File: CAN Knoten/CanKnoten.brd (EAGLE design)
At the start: 112.9 x 61.3 mm, 43 parts, among them IC1 74LS165D, IC2 74LS165D, K1 68711614522, K2 68711614522, K3 68711614522, K4 68711614522, Q1 HC49-U - 16MHz, Q2 HC49-U - xMHz

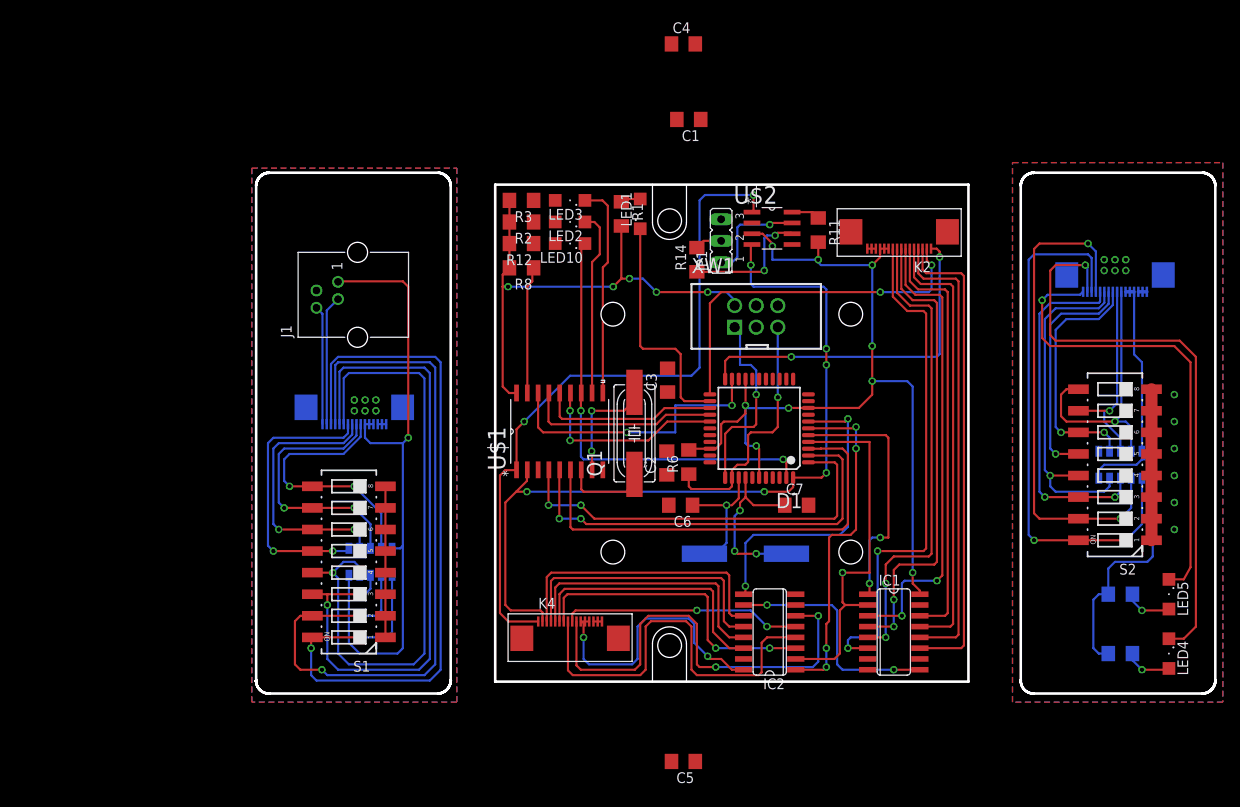
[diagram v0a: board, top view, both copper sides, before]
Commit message: 
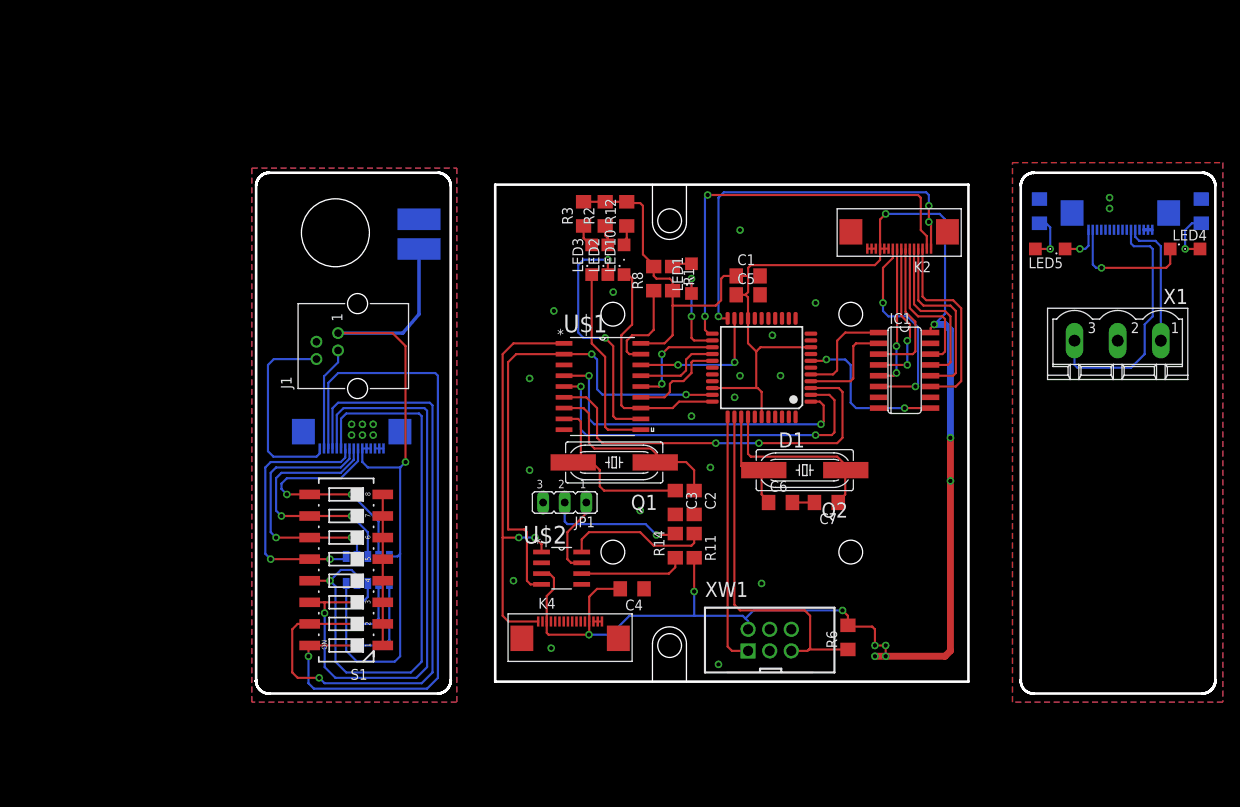
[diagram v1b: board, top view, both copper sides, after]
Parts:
- removed IC2: 74LS165D, 74xx-us:SO16
- removed RN1: (no value), resistor-array:745-10
- removed S2: 219-08, switch-dil:CTS-219-08
- added PAD1, PAD2: (no value), wirepad:SMD2,54-5,08
- added X1: MSTBV3, con-phoenix-508:MSTBV3
- moved C4 64.4 mm to (62.9, -29.2), turned to 180 degrees
- moved C5 55.5 mm to (76.5, 5.40), turned to 0 degrees
- moved R4 52.9 mm to (129.9, 15.2), turned to 90 degrees
- moved LED4 47.7 mm to (128.0, 10.8), turned to 0 degrees
- moved U$2 47.1 mm to (54.6, -26.8)
- moved R5 46.1 mm to (110.8, 15.2), turned to 90 degrees
- moved LED5 43.0 mm to (112.1, 10.8), turned to 180 degrees
- moved R11 39.9 mm to (70.2, -24.1)
- moved XW1 38.1 mm to (79.1, -35.2)
- moved JP1 35.9 mm to (54.9, -19.1), turned to 180 degrees
- moved R14 33.8 mm to (67.9, -24.1)
- moved IC1 30.8 mm to (94.9, -3.49)
- moved R6 27.9 mm to (88.3, -34.9)
- moved C1 19.7 mm to (76.5, 7.62), turned to 0 degrees
- moved U$4 19.1 mm to (95.2, -29.2)
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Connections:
- net N$31 renamed PDI_RESET
- net N$33 renamed REAR_MCP2515_TXCAN
- net N$34 renamed REAR_MCP2515_RXCAN
- removed net 74XX165_SH/LD_IC2: D1.6, IC2.1
- removed net CAN_BITRATE_0: IC2.11, K4.3
- removed net CAN_BITRATE_1: IC2.12, K4.4
- removed net CAN_BITRATE_2: IC2.13, K4.5
- removed net CAN_BITRATE_3: IC2.14, K4.6
- removed net CAN_BITRATE_4: IC2.3, K4.7
- removed net CAN_BITRATE_5: IC2.4, K4.8
- removed net CAN_BITRATE_6: IC2.5, K4.9
- removed net CAN_BITRATE_7: IC2.6, K4.10
- removed net N$13: D1.40
- removed net N$14: D1.41
- removed net N$18: D1.42
- removed net N$19: K3.9, RN1.8, S2.10
- removed net N$2: IC1.9, IC2.10
- removed net N$20: D1.28
- removed net N$21: D1.29
- removed net N$30: K3.10, RN1.9, S2.9
- removed net N$4: K3.3, RN1.1, S2.16
- removed net N$5: K3.4, RN1.2, S2.15
- removed net N$6: K3.5, RN1.3, S2.14
- removed net N$7: K3.6, RN1.4, S2.13
- removed net N$8: K3.7, RN1.6, S2.12
- removed net N$9: K3.8, RN1.7, S2.11
- new net REAR_CANH: K3.12, X1.1
- new net REAR_CANL: K3.11, X1.3
- net 74XX165_CLK: no longer IC2.2
- net 74XX165_OUT: now also IC1.9; no longer IC2.9
- net FRONT_GND: now also PAD1.1
- net FRONT_VCC: now also PAD2.1
- net GND: now also IC1.10; no longer IC2.15, IC2.8
- net MCP2515_INT: now also D1.33; no longer D1.43
- net MCP2515_RXCAN: now also D1.32; no longer D1.44
- net REAR_GND: now also X1.2; no longer S2.1, S2.2, S2.3, S2.4, S2.5, S2.6, S2.7, S2.8
- net REAR_VCC: now also K3.3; no longer K3.11, K3.12, RN1.10, RN1.5
- net VCC: now also K4.3; no longer IC2.16, K4.11, K4.12
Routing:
- net N$4: track 64.0 -> 0.00 mm, vias 2 -> 0
- net N$5: track 59.5 -> 0.00 mm, vias 2 -> 0
- net REAR_VCC: track 58.6 -> 0.00 mm
- net REAR_MCP2515_RXCAN: track 69.0 -> 15.3 mm
- net CAN_BITRATE_7: track 52.8 -> 0.00 mm, vias 2 -> 0
- net REAR_MCP2515_TXCAN: track 55.8 -> 4.79 mm
- net CAN_BITRATE_5: track 47.9 -> 0.00 mm
- net N$6: track 41.5 -> 0.00 mm, vias 2 -> 0
- net N$7: track 40.8 -> 0.00 mm, vias 1 -> 0
- net 74XX165_SH/LD_IC2: track 40.4 -> 0.00 mm, vias 4 -> 0
- net NODE_ID_6: track 55.5 -> 16.9 mm
- net VCC: track 199.5 -> 237.9 mm, vias 16 -> 11
- net MCP2515_RXCAN: track 96.3 -> 58.1 mm, vias 6 -> 2
- net NODE_ID_4: track 54.9 -> 17.1 mm, vias 2 -> 0
- net NODE_ID_5: track 55.3 -> 17.6 mm
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
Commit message: 
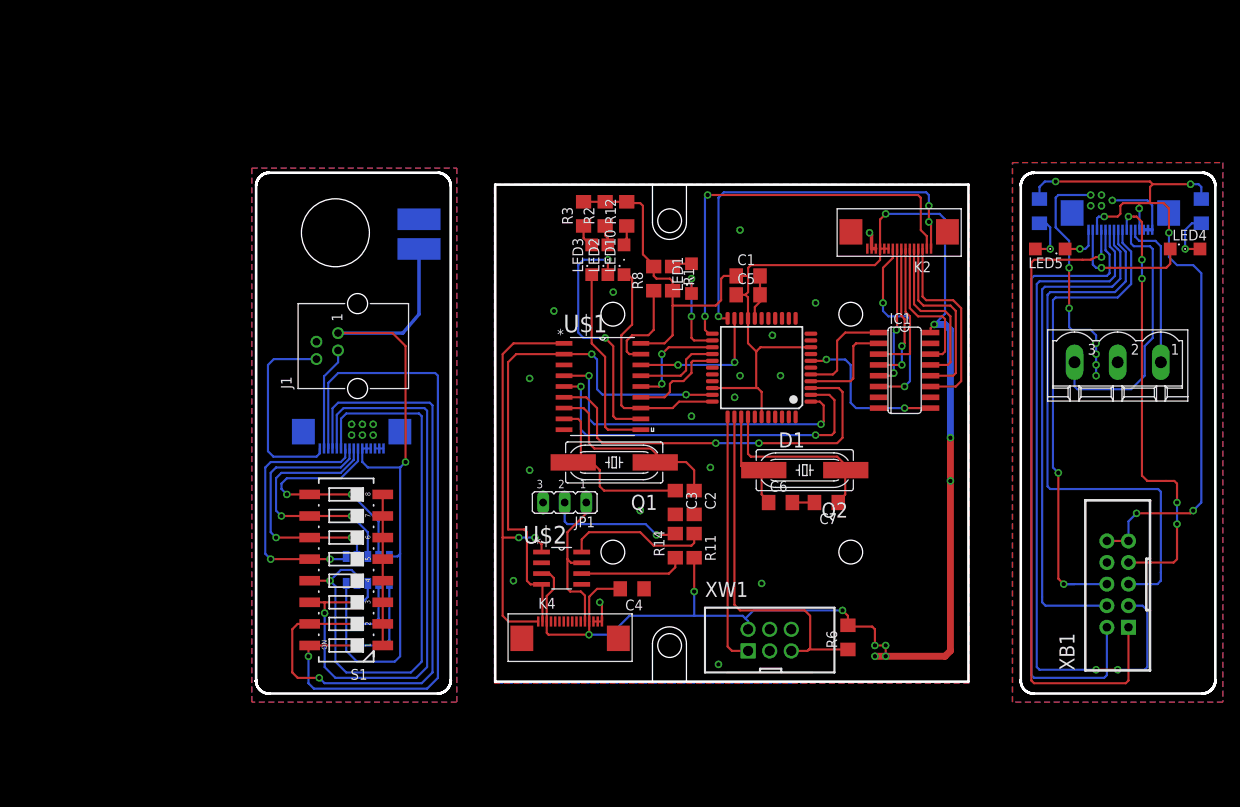
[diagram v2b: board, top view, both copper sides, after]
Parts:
- added XB1: (no value), Wannenstiftleisten:WSL10
- moved X1 2.54 mm to (120.0, -2.54)
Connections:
- removed net N$17: C6.2, C7.2
- new net EXTENDED_I2C_SCL: D1.11, K4.7
- new net EXTENDED_I2C_SDA: D1.10, K4.6
- new net EXTENDED_SPI_MISO: D1.16, K4.8
- new net EXTENDED_SPI_MOSI: D1.15, K4.9
- new net EXTENDED_SPI_SCK: D1.17, K4.10
- new net EXTENDED_UART_RXD: D1.12, K4.4
- new net EXTENDED_UART_TXD: D1.13, K4.5
- new net N$2: K3.4, XB1.1
- new net N$4: K3.5, XB1.2
- new net N$5: K3.6, XB1.3
- new net N$6: K3.7, XB1.4
- new net N$7: K3.8, XB1.5
- new net N$8: K3.9, XB1.6
- new net N$9: K3.10, XB1.7
- net GND: now also C6.2, C7.2
- net MCP2551_CANH: now also K4.12
- net MCP2551_CANL: now also K4.11
- net REAR_GND: now also XB1.8
- net REAR_VCC: now also XB1.10, XB1.9
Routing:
- net REAR_VCC: track 0.00 -> 91.0 mm, vias 0 -> 7
- net N$5: track 0.00 -> 82.8 mm, vias 0 -> 2
- net N$2: track 0.00 -> 78.8 mm, vias 0 -> 1
- net N$4: track 0.00 -> 76.2 mm
- net N$7: track 0.00 -> 66.9 mm
- net N$6: track 0.00 -> 60.4 mm
- net N$8: track 0.00 -> 57.1 mm, vias 0 -> 2
- net N$9: track 0.00 -> 52.7 mm, vias 0 -> 5
- net REAR_GND: track 1.00 -> 37.3 mm, vias 2 -> 11
- net GND: track 2.00 -> 13.8 mm, vias 17 -> 18
- net MCP2551_CANH: track 9.67 -> 18.6 mm
- net MCP2515_RXCAN: track 58.1 -> 62.5 mm
- net N$17: track 2.60 -> 0.00 mm
- net REAR_CANL: track 29.1 -> 31.7 mm
- net REAR_CANH: track 15.4 -> 18.0 mm
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- added copper zone on layer 1, net GND
- added copper zone on layer 16, net GND
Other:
- board text added: "CAN-H"
- board text added: "CAN-L"
- board text added: "GND"

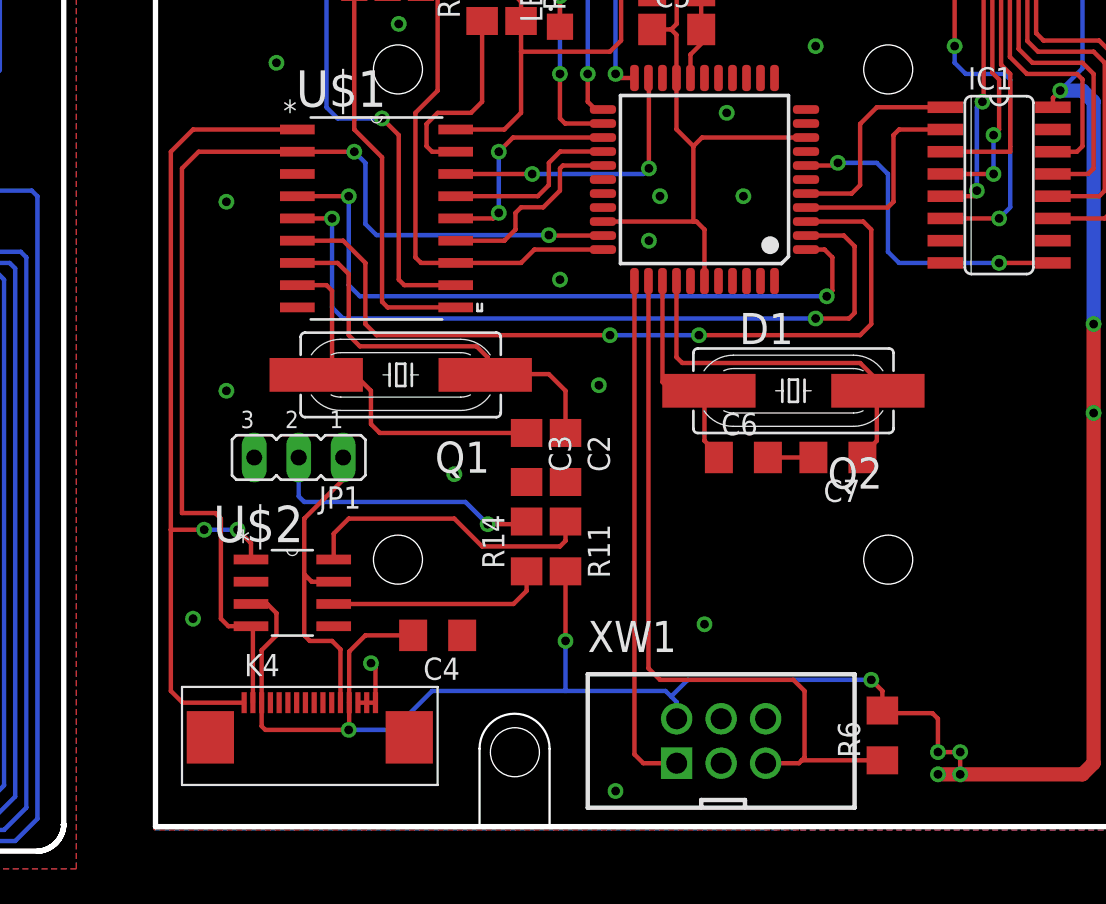
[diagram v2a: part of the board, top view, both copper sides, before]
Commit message: 
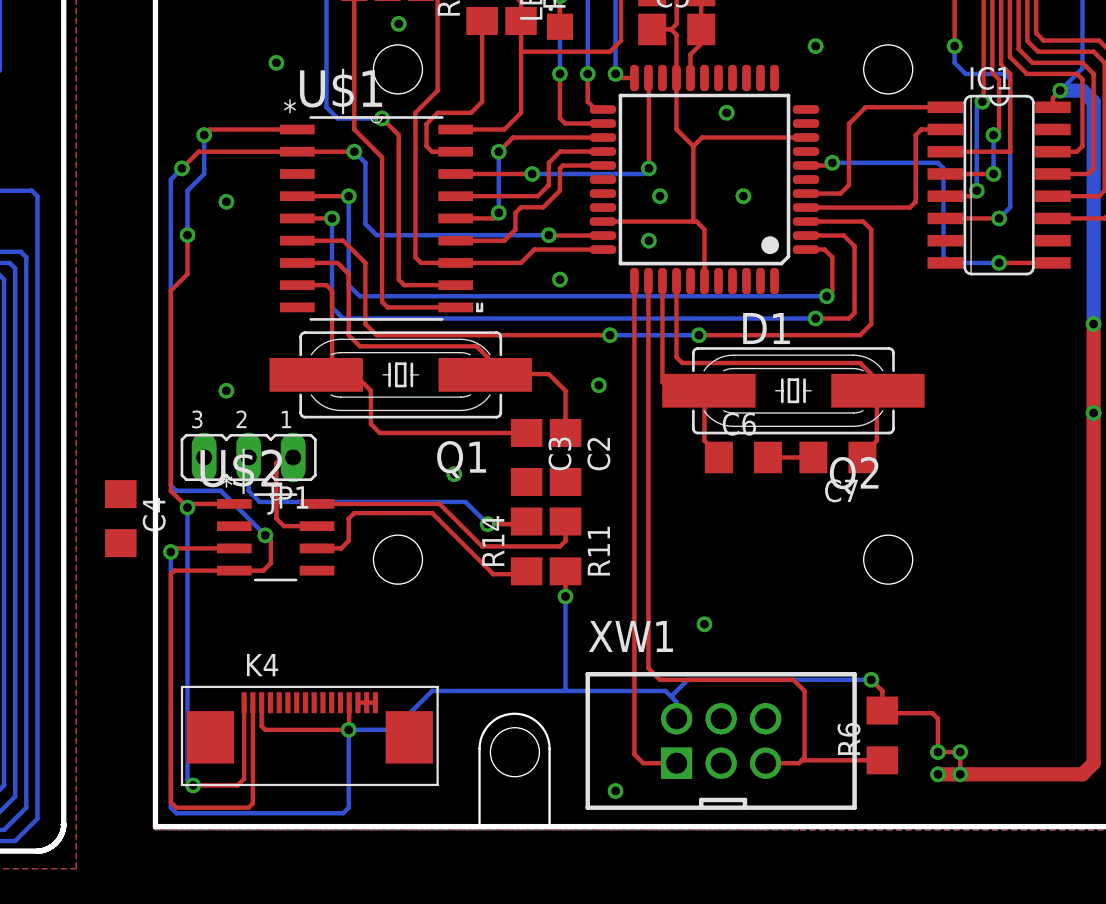
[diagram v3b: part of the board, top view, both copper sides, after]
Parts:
- moved C4 19.3 mm to (44.8, -22.5), turned to 270 degrees
- moved U$2 3.31 mm to (53.6, -23.6)
- moved JP1 2.86 mm to (52.1, -19.1)
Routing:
- net MCP2515_RXCAN: track 62.5 -> 84.8 mm, vias 2 -> 4
- net VCC: track 237.9 -> 257.0 mm, vias 11 -> 12
- net MCP2551_CANH: track 18.6 -> 6.75 mm
- net MCP2515_TXCAN: track 48.8 -> 54.1 mm, vias 2 -> 4
- net N$12: track 16.0 -> 18.6 mm
- net MCP2551_CANL: track 12.4 -> 15.1 mm
- net GND: track 13.8 -> 11.5 mm, vias 18 -> 16
- net MCP2551_RS: track 17.0 -> 16.4 mm

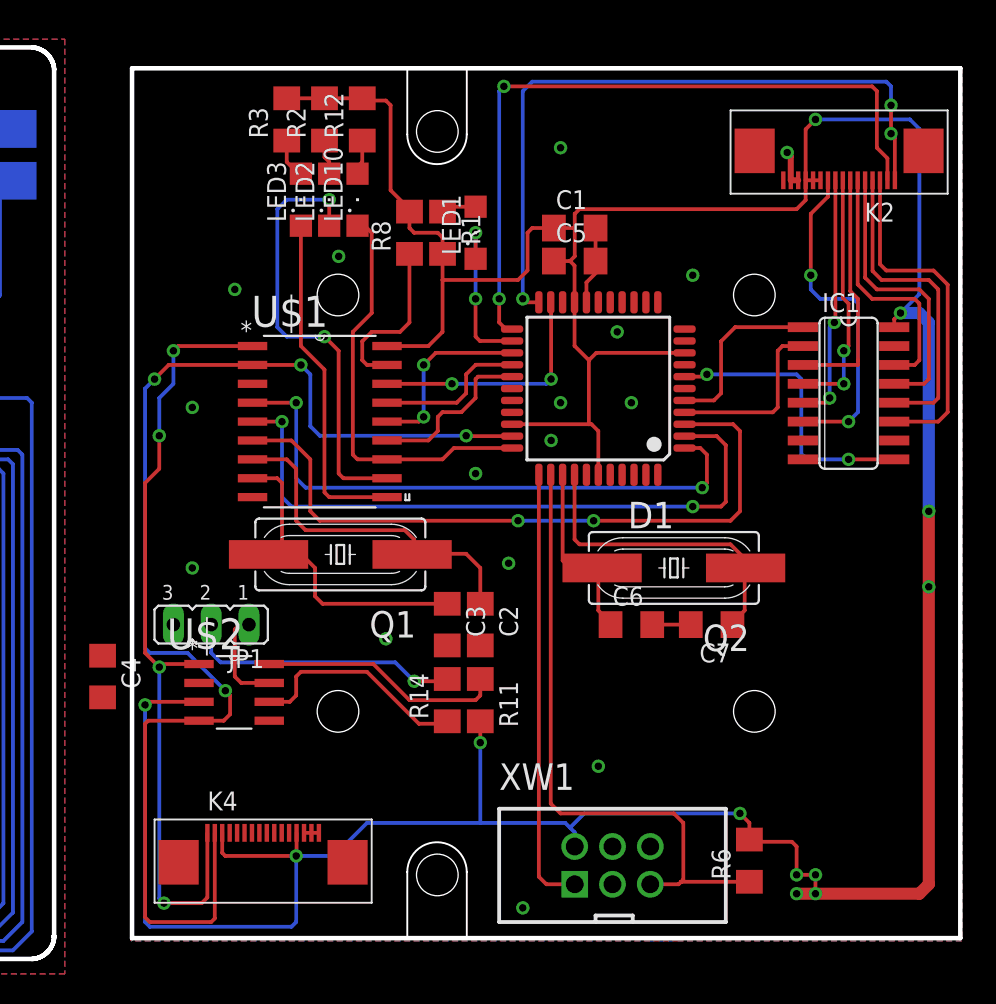
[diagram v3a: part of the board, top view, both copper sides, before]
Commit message: 
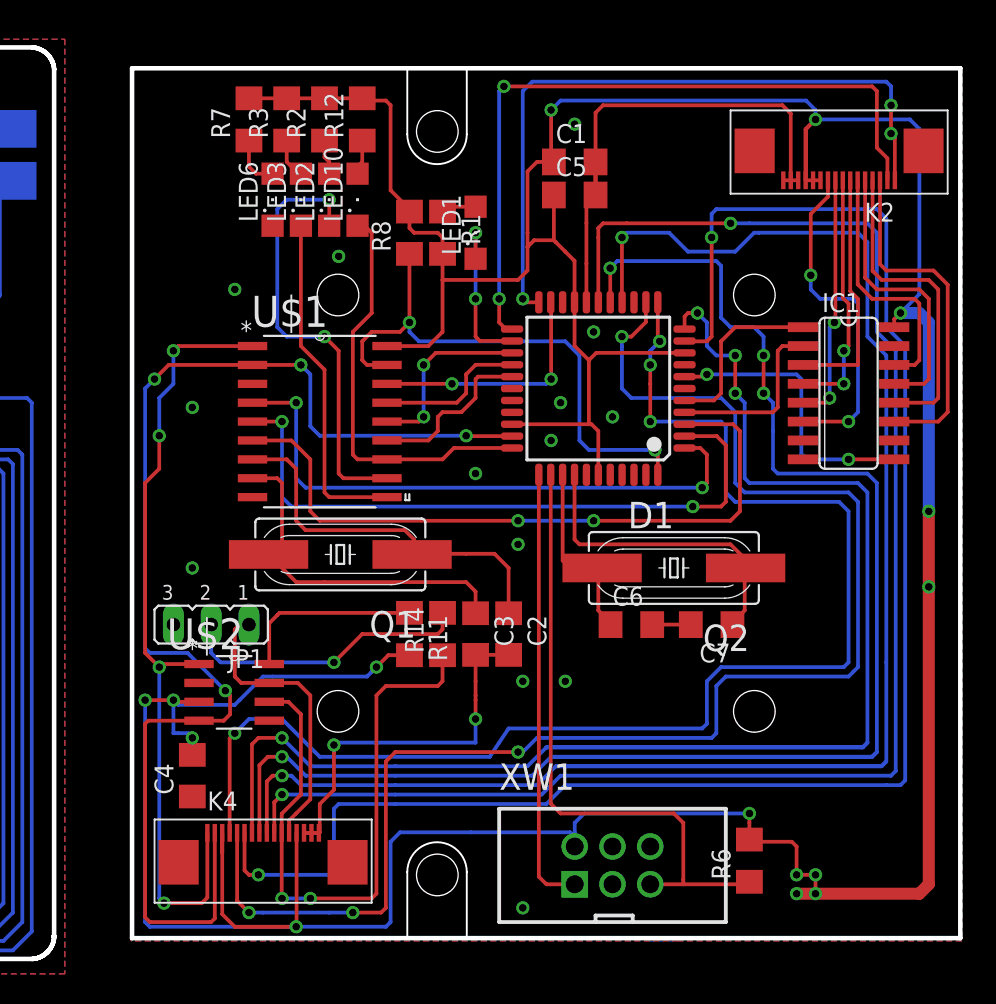
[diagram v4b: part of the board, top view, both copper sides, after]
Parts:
- added LED6: (no value), led:SML1206
- added R7: 560R, rcl:R1206
- moved C4 8.99 mm to (50.8, -29.2), turned to 90 degrees
- moved R11 6.51 mm to (65.4, -19.7)
- moved R14 4.46 mm to (67.6, -19.7)
- moved C1 4.44 mm to (76.5, 12.1)
- moved C5 4.44 mm to (76.5, 9.84)
- moved C2 2.01 mm to (72.1, -19.7)
- moved C3 2.01 mm to (69.8, -19.7)
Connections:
- new net N$13: LED6.A, R7.1
- net MCP2515_CLKOUT: now also LED6.C
- net MCP2515_RESET: now also D1.44
- net VCC: now also R7.2
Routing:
- net EXTENDED_SPI_MOSI: track 0.00 -> 126.3 mm, vias 0 -> 2
- net EXTENDED_SPI_MISO: track 0.00 -> 121.1 mm, vias 0 -> 4
- net EXTENDED_I2C_SDA: track 0.00 -> 112.8 mm, vias 0 -> 2
- net EXTENDED_I2C_SCL: track 0.00 -> 111.1 mm, vias 0 -> 4
- net EXTENDED_SPI_SCK: track 0.00 -> 105.6 mm, vias 0 -> 2
- net EXTENDED_UART_TXD: track 0.00 -> 100.9 mm, vias 0 -> 4
- net EXTENDED_UART_RXD: track 0.00 -> 91.0 mm, vias 0 -> 4
- net GND: track 11.5 -> 62.9 mm
- net VCC: track 257.0 -> 301.5 mm, vias 12 -> 15
- net MCP2551_CANL: track 15.1 -> 41.8 mm, vias 0 -> 2
- net MCP2515_RESET: track 11.4 -> 36.9 mm, vias 0 -> 2
- net MCP2551_CANH: track 6.75 -> 19.7 mm
- net MCP2515_OSC1: track 21.6 -> 25.6 mm
- net MCP2551_RS: track 16.4 -> 12.5 mm
- net N$13: track 0.00 -> 3.54 mm
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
